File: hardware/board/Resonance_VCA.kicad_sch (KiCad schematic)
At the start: 33 parts, among them Q601 BCM847, U4 TL074

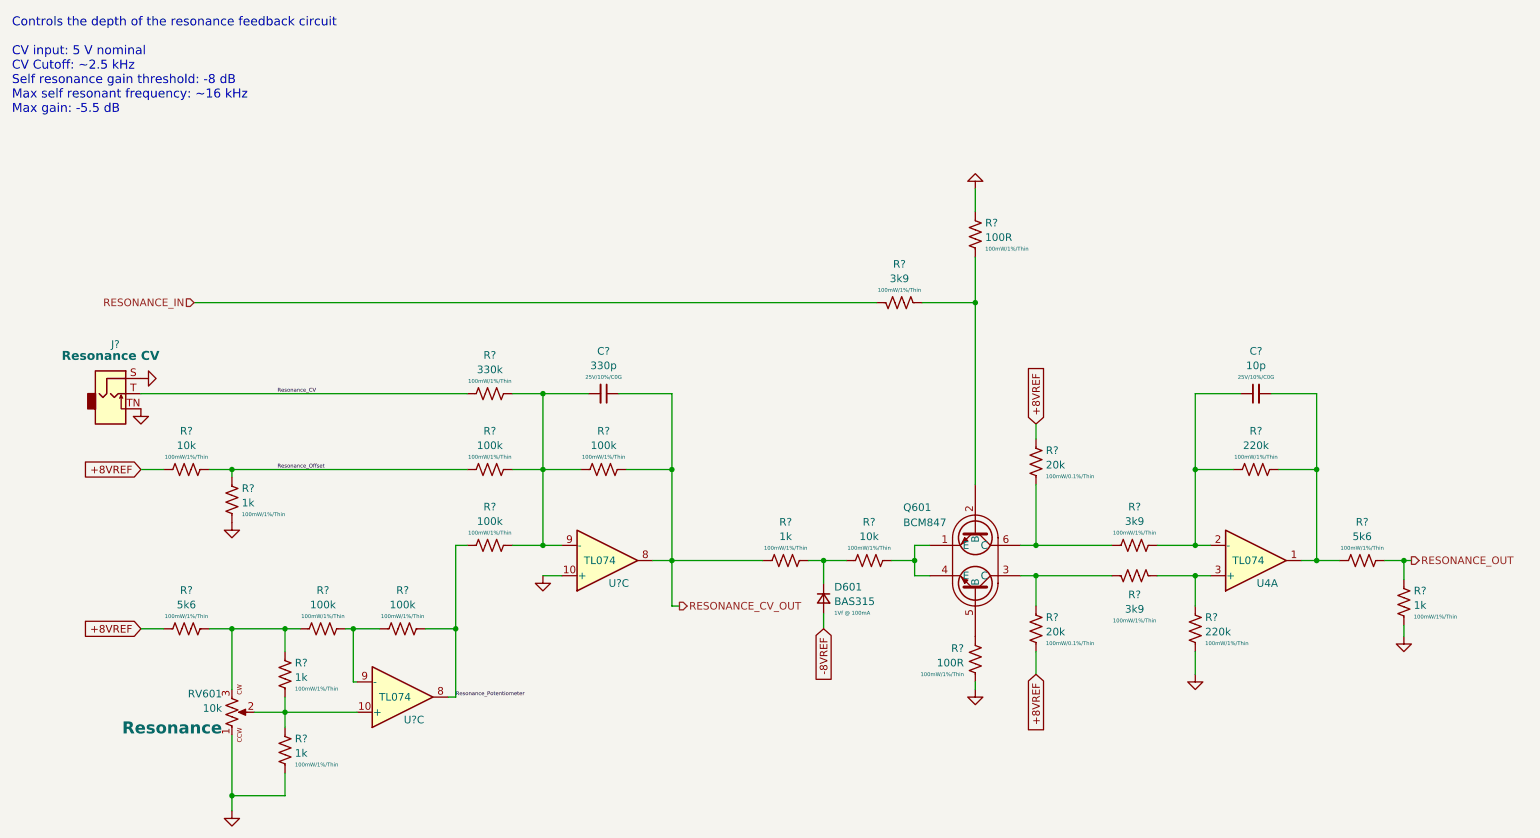
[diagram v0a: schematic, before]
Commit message: update board to kicad 9
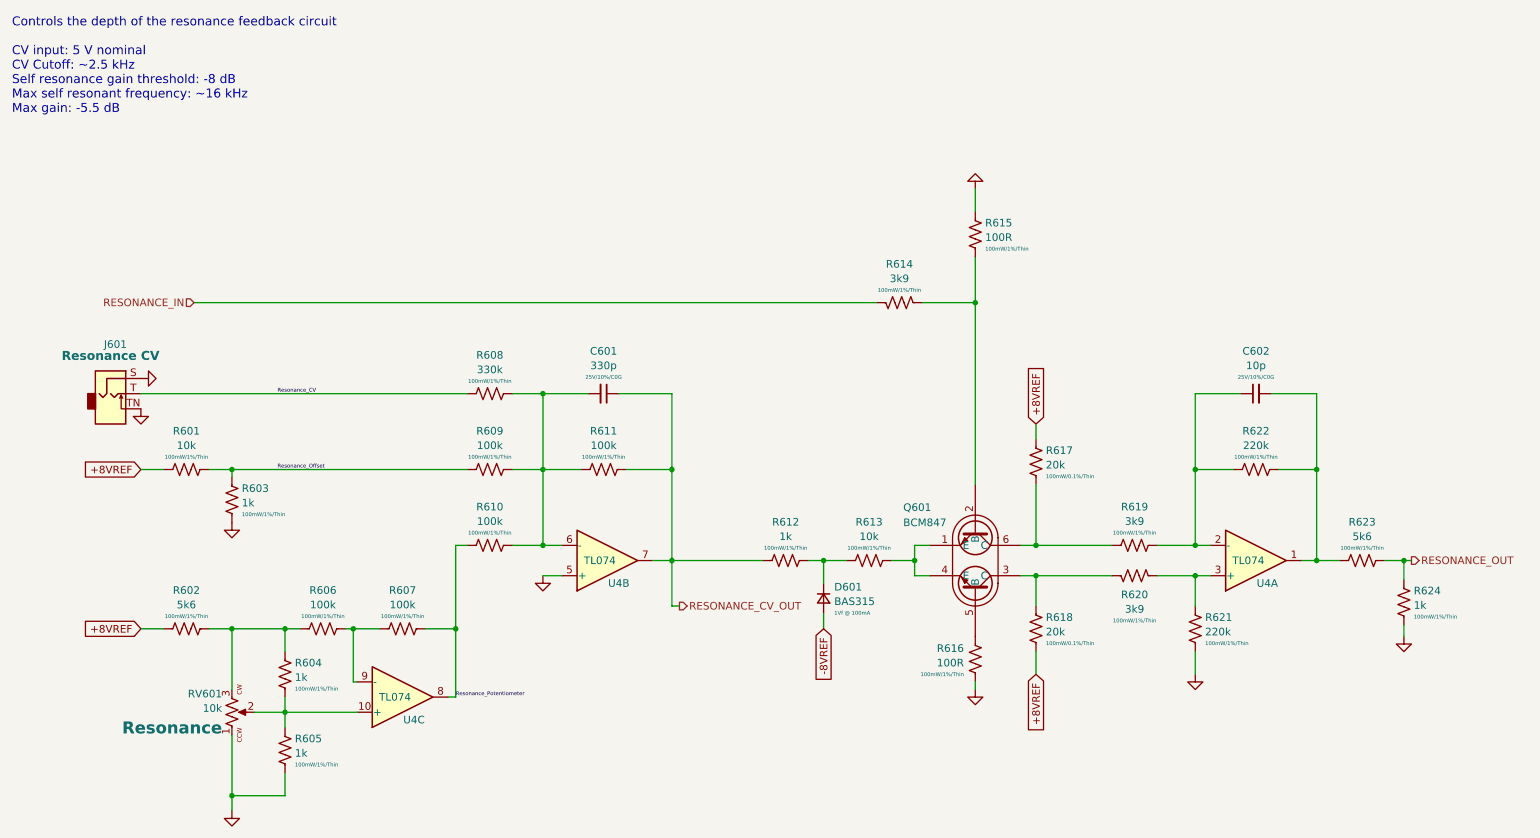
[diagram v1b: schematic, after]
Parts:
- gave numbers to parts that had none: 28
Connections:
- net GND: now also U4.5 (+); no longer U4.10 (+)
- net RESONANCE_CV_OUT: now also U4.7; no longer U4.8
- net at C601.2, R608.1, R609.1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: now also U4.6 (-); no longer U4.9 (-)
